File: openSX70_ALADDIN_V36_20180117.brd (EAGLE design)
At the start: 95.9 x 27.9 mm, 42 parts, among them Q1 5.8A/30V/35mΩ, Q2 5.8A/30V/35mΩ, U1 ATMEGA328P_TQFP, U3 BH1750FVI-TR, Y1 CSTCE16M0V53-R0

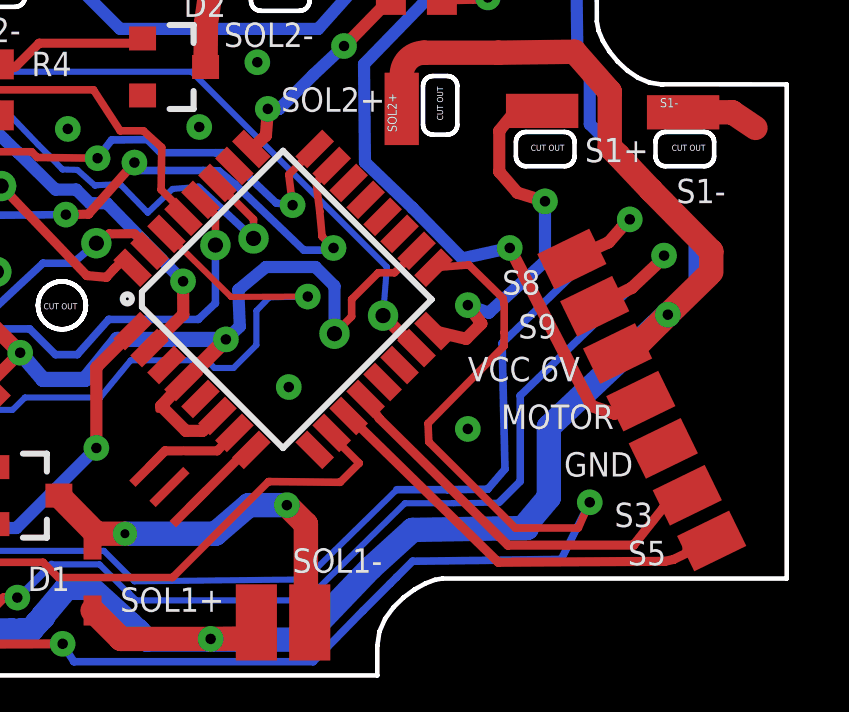
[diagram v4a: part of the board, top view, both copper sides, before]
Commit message: Added TP to pins 15 16 and 17, for bootloader programming (?)
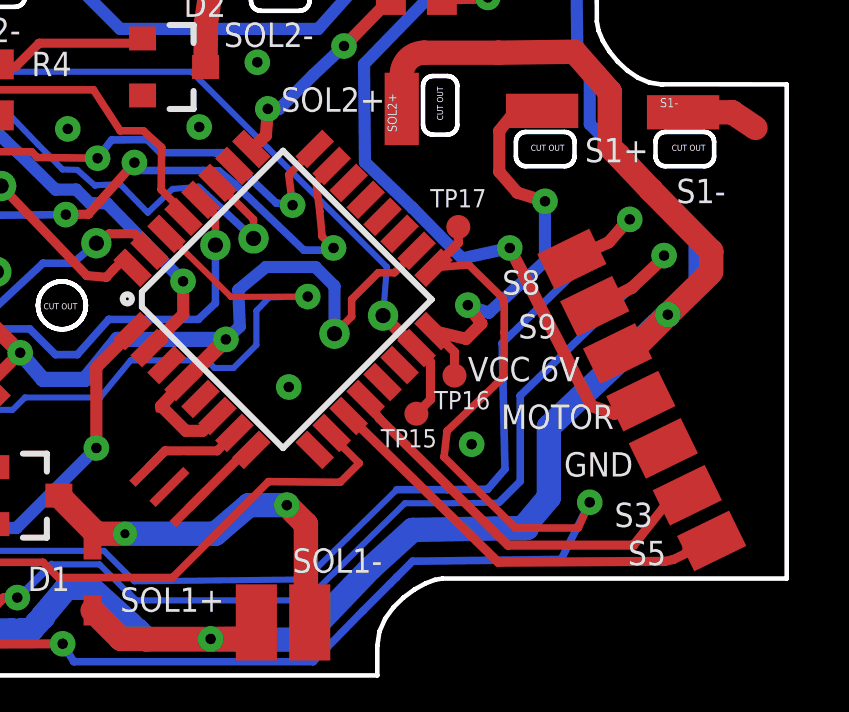
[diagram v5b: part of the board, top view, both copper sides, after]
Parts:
- added TP15, TP16, TP17: PTR1TP08R, testpad:TP08R
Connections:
- net LED: now also TP17.TP
- net S1: now also TP16.TP
- net SOL2: now also TP15.TP
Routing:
- net SOL2: track 26.3 -> 28.9 mm
- net S1: track 12.9 -> 14.7 mm
- net LED: track 92.3 -> 93.6 mm
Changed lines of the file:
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@@
 <element name="TP-3.3V" library="openSX70" package="SX70-S-PAD2" value="SX70-S-PAD-NEW" x="14.351" y="4.064" rot="R90"/>
 <element name="TP-GND" library="openSX70" package="SX70-S-PAD2" value="SX70-S-PAD-NEW" x="12.192" y="4.064" rot="R90"/>
+<element name="TP15" library="testpad" library_urn="urn:adsk.eagle:library:385" package="TP08R" package3d_urn="urn:adsk.eagle:package:27956/1" value="PTR1TP08R" x="85.598" y="11.938" smashed="yes">
+<attribute name="NAME" x="84.409" y="10.8141" size="0.6096" layer="25" font="vector" ratio="12"/>
+<attribute name="TP_SIGNAL_NAME" value="" x="85.598" y="10.033" size="1" layer="37"/>
+<attribute name="VALUE" x="85.217" y="11.557" size="0.0254" layer="27"/>
+</element>
+<element name="TP16" library="testpad" library_urn="urn:adsk.eagle:library:385" package="TP08R" package3d_urn="urn:adsk.eagle:package:27956/1" value="PTR1TP08R" x="86.868" y="13.208" smashed="yes">
+<attribute name="NAME" x="86.187" y="12.0841" size="0.6096" layer="25" font="vector" ratio="12"/>
+<attribute name="TP_SIGNAL_NAME" value="" x="86.868" y="11.303" size="1" layer="37"/>
+<attribute name="VALUE" x="86.487" y="12.827" size="0.0254" layer="27"/>
+</element>
+<element name="TP17" library="testpad" library_urn="urn:adsk.eagle:library:385" package="TP08R" package3d_urn="urn:adsk.eagle:package:27956/1" value="PTR1TP08R" x="86.995" y="18.161" smashed="yes">
+<attribute name="NAME" x="86.06" y="18.8151" size="0.6096" layer="25" font="vector" ratio="12"/>
+<attribute name="TP_SIGNAL_NAME" value="" x="86.995" y="16.256" size="1" layer="37"/>
+<attribute name="VALUE" x="86.614" y="17.78" size="0.0254" layer="27"/>
+</element>
 </elements>
 <signals>
@@
 <wire x1="88.9" y1="22.0345" x2="89.789" y2="22.032" width="0.4064" layer="1"/>
 <wire x1="88.36025" y1="20.0025" x2="88.36025" y2="21.36775" width="0.4064" layer="1"/>
+<contactref element="TP16" pad="TP"/>
+<wire x1="86.168225" y1="14.692571875" x2="86.868" y2="13.992796875" width="0.3048" layer="1"/>
+<wire x1="86.868" y1="13.992796875" x2="86.868" y2="13.208" width="0.3048" layer="1"/>
 </signal>
 <signal name="LED">
@@
 <wire x1="90.9955" y1="8.128" x2="88.9" y2="8.128" width="0.254" layer="1"/>
 <wire x1="90.9955" y1="8.128" x2="91.3765" y2="8.98525" width="0.254" layer="1"/>
-<wire x1="88.52423125" y1="14.64641875" x2="88.519" y2="14.19225" width="0.254" layer="1"/>
-<wire x1="88.519" y1="14.19225" x2="85.98535" y2="11.61415" width="0.254" layer="1"/>
-<wire x1="86.01075" y1="10.99873125" x2="85.98535" y2="11.61415" width="0.254" layer="1"/>
-<wire x1="88.9" y1="8.128" x2="86.01075" y2="10.99873125" width="0.254" layer="1"/>
+<wire x1="88.52423125" y1="14.64641875" x2="88.519" y2="13.17625" width="0.254" layer="1"/>
+<wire x1="88.519" y1="13.17625" x2="86.62035" y2="11.36015" width="0.254" layer="1"/>
+<wire x1="86.51875" y1="10.49073125" x2="86.62035" y2="11.36015" width="0.254" layer="1"/>
+<wire x1="88.9" y1="8.128" x2="86.51875" y2="10.49073125" width="0.254" layer="1"/>
 <wire x1="82.1569" y1="3.6709" x2="83.82" y2="5.3717875" width="0.254" layer="16"/>
 <wire x1="68.1355" y1="1.99225" x2="70.2945" y2="4.2545" width="0.3048" layer="1"/>
+<contactref element="TP17" pad="TP"/>
+<wire x1="86.995" y1="18.161" x2="86.995" y2="17.6302" width="0.3048" layer="1"/>
+<wire x1="86.995" y1="17.6302" x2="86.168225" y2="16.803425" width="0.3048" layer="1"/>
 </signal>
 <signal name="S3">
@@
 <via x="67.31" y="23.8125" extent="1-16" drill="0.508"/>
 <via x="84.48675" y="15.20825" extent="1-16" drill="0.508"/>
+<contactref element="TP15" pad="TP"/>
+<wire x1="85.6025375" y1="14.126884375" x2="86.0679" y2="13.661521875" width="0.3048" layer="1"/>
+<wire x1="86.0679" y1="12.4079" x2="85.598" y2="11.938" width="0.3048" layer="1"/>
+<wire x1="86.0679" y1="13.661521875" x2="86.0679" y2="12.4079" width="0.3048" layer="1"/>
 </signal>
 <signal name="FF">
@@
 <via x="23.495" y="17.78" extent="1-16" drill="0.35"/>
 <via x="22.0345" y="22.0345" extent="1-16" drill="0.35"/>
-<via x="87.3125" y="11.43" extent="1-16" drill="0.35"/>
+<via x="87.4395" y="10.922" extent="1-16" drill="0.35"/>
 <via x="83.08975" y="26.9875" extent="1-16" drill="0.35"/>
 <wire x1="16.41475" y1="9.652" x2="16.5693" y2="9.5279" width="0.2032" layer="16"/>

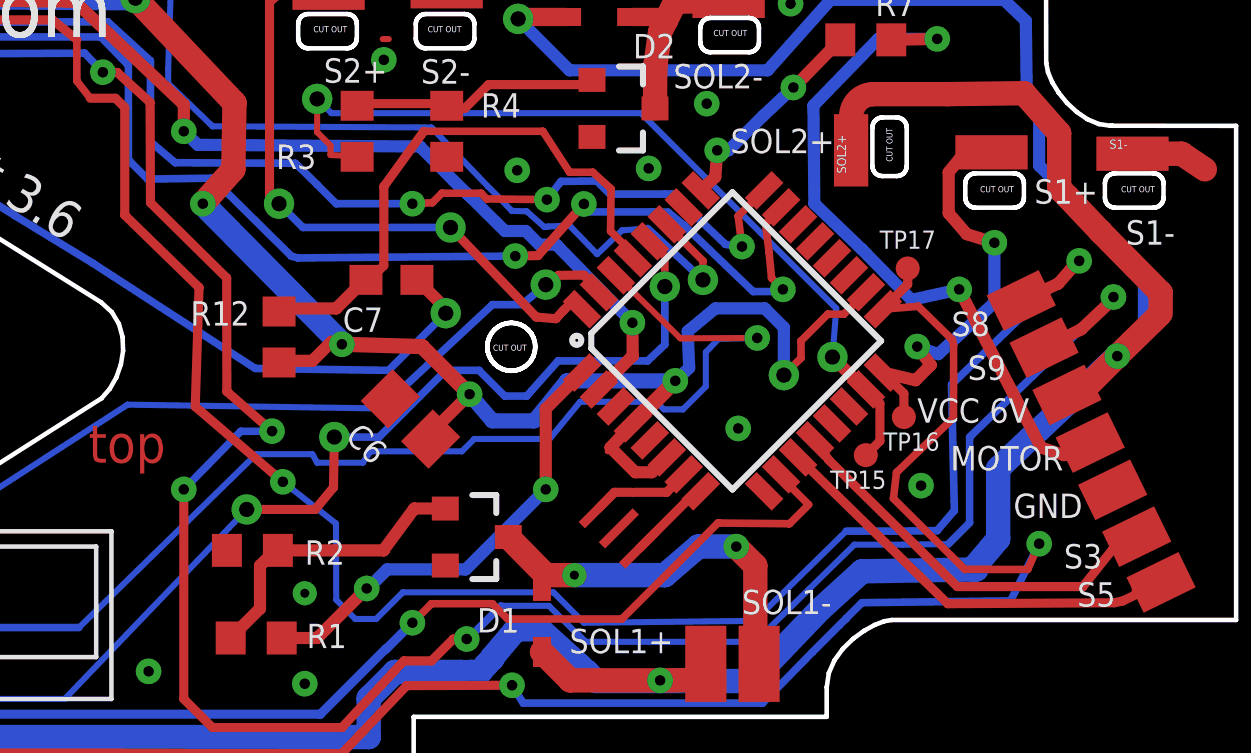
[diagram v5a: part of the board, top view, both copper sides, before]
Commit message: Minor fixes, making the board look nicer.
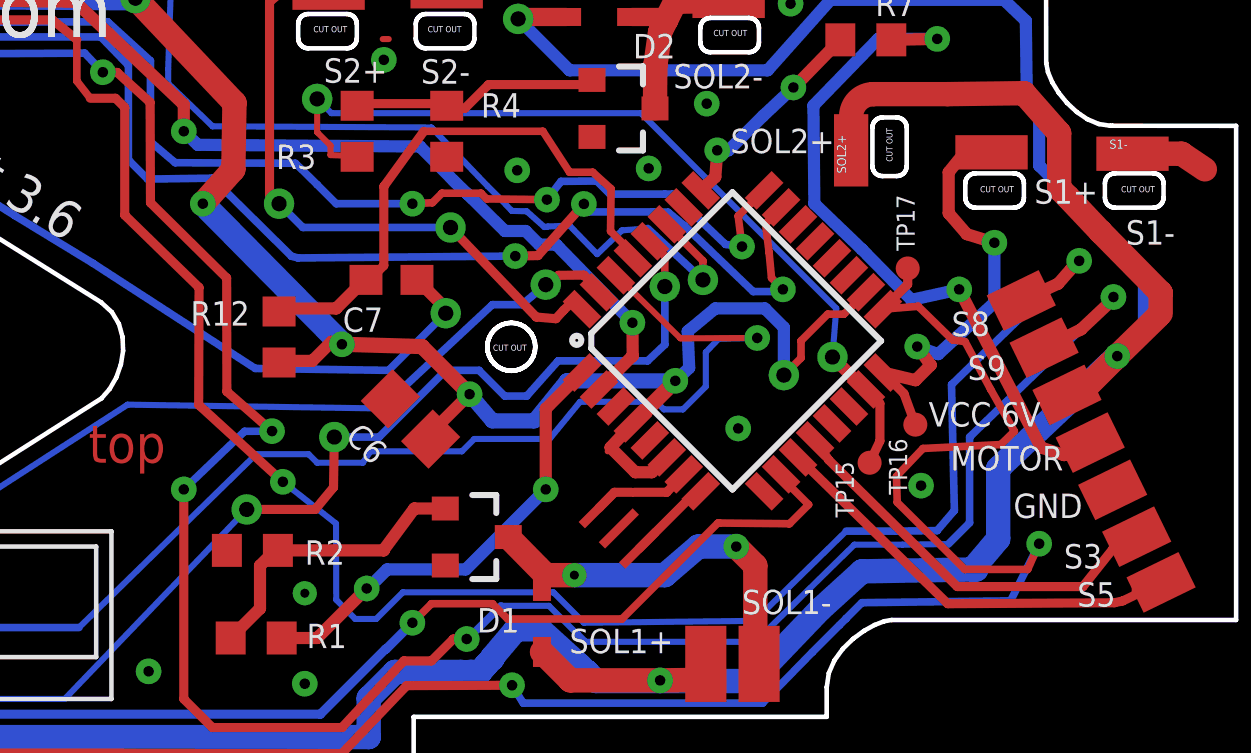
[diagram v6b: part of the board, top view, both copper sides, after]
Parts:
- moved TP16 0.46 mm to (87.2, 13.0)
- moved TP15 0.28 mm to (85.7, 11.7)
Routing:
- net LED: track 93.6 -> 96.5 mm
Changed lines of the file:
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@@
 <text x="90.51925" y="9.8425" size="0.8128" layer="21" font="vector" ratio="20">GND</text>
 <text x="88.42375" y="11.43" size="0.8128" layer="21" font="vector" ratio="20">MOTOR</text>
-<text x="87.3125" y="13.0175" size="0.8128" layer="21" font="vector" ratio="20">VCC 6V</text>
+<text x="87.6935" y="12.8905" size="0.8128" layer="21" font="vector" ratio="20">VCC 6V</text>
 <text x="88.99525" y="14.44625" size="0.8128" layer="21" font="vector" ratio="20">S9</text>
 <text x="88.4555" y="15.90675" size="0.8128" layer="21" font="vector" ratio="20">S8</text>
@@
 <wire x1="59.944" y1="5.207" x2="55.88" y2="5.207" width="0.1524" layer="21"/>
 <wire x1="55.88" y1="5.207" x2="55.88" y2="8.89" width="0.1524" layer="21"/>
+<text x="41.3385" y="24.79675" size="1.27" layer="22" font="vector" ratio="15" rot="R212">"aladdin"</text>
 </plain>
 <attributes>
@@
 <element name="TP-3.3V" library="openSX70" package="SX70-S-PAD2" value="SX70-S-PAD-NEW" x="14.351" y="4.064" rot="R90"/>
 <element name="TP-GND" library="openSX70" package="SX70-S-PAD2" value="SX70-S-PAD-NEW" x="12.192" y="4.064" rot="R90"/>
-<element name="TP15" library="testpad" library_urn="urn:adsk.eagle:library:385" package="TP08R" package3d_urn="urn:adsk.eagle:package:27956/1" value="PTR1TP08R" x="85.598" y="11.938" smashed="yes">
-<attribute name="NAME" x="84.409" y="10.8141" size="0.6096" layer="25" font="vector" ratio="12"/>
-<attribute name="TP_SIGNAL_NAME" value="" x="85.598" y="10.033" size="1" layer="37"/>
-<attribute name="VALUE" x="85.217" y="11.557" size="0.0254" layer="27"/>
-</element>
-<element name="TP16" library="testpad" library_urn="urn:adsk.eagle:library:385" package="TP08R" package3d_urn="urn:adsk.eagle:package:27956/1" value="PTR1TP08R" x="86.868" y="13.208" smashed="yes">
-<attribute name="NAME" x="86.187" y="12.0841" size="0.6096" layer="25" font="vector" ratio="12"/>
-<attribute name="TP_SIGNAL_NAME" value="" x="86.868" y="11.303" size="1" layer="37"/>
-<attribute name="VALUE" x="86.487" y="12.827" size="0.0254" layer="27"/>
+<element name="TP15" library="testpad" library_urn="urn:adsk.eagle:library:385" package="TP08R" package3d_urn="urn:adsk.eagle:package:27956/1" value="PTR1TP08R" x="85.725" y="11.684" smashed="yes">
+<attribute name="NAME" x="85.1979" y="9.86" size="0.6096" layer="25" font="vector" ratio="12" rot="R90"/>
+<attribute name="TP_SIGNAL_NAME" value="" x="85.725" y="9.779" size="1" layer="37"/>
+<attribute name="VALUE" x="85.344" y="11.303" size="0.0254" layer="27"/>
+</element>
+<element name="TP16" library="testpad" library_urn="urn:adsk.eagle:library:385" package="TP08R" package3d_urn="urn:adsk.eagle:package:27956/1" value="PTR1TP08R" x="87.249" y="12.954" smashed="yes">
+<attribute name="NAME" x="86.9759" y="10.622" size="0.6096" layer="25" font="vector" ratio="12" rot="R90"/>
+<attribute name="TP_SIGNAL_NAME" value="" x="87.249" y="11.049" size="1" layer="37"/>
+<attribute name="VALUE" x="86.868" y="12.573" size="0.0254" layer="27"/>
 </element>
 <element name="TP17" library="testpad" library_urn="urn:adsk.eagle:library:385" package="TP08R" package3d_urn="urn:adsk.eagle:package:27956/1" value="PTR1TP08R" x="86.995" y="18.161" smashed="yes">
-<attribute name="NAME" x="86.06" y="18.8151" size="0.6096" layer="25" font="vector" ratio="12"/>
+<attribute name="NAME" x="87.2299" y="18.75" size="0.6096" layer="25" font="vector" ratio="12" rot="R90"/>
 <attribute name="TP_SIGNAL_NAME" value="" x="86.995" y="16.256" size="1" layer="37"/>
 <attribute name="VALUE" x="86.614" y="17.78" size="0.0254" layer="27"/>
@@
 <contactref element="TP16" pad="TP"/>
 <wire x1="86.168225" y1="14.692571875" x2="86.868" y2="13.992796875" width="0.3048" layer="1"/>
-<wire x1="86.868" y1="13.992796875" x2="86.868" y2="13.208" width="0.3048" layer="1"/>
+<wire x1="86.868" y1="13.992796875" x2="87.249" y2="12.954" width="0.3048" layer="1"/>
 </signal>
 <signal name="LED">
@@
 <wire x1="90.424" y1="7.08025" x2="91.3765" y2="8.98525" width="0.254" layer="16"/>
 <wire x1="87.34425" y1="16.898675" x2="88.48725" y2="15.77975" width="0.254" layer="1"/>
-<wire x1="88.48725" y1="15.77975" x2="88.52423125" y2="15.59448125" width="0.254" layer="1"/>
-<wire x1="88.52423125" y1="15.59448125" x2="88.52423125" y2="14.64641875" width="0.254" layer="1"/>
+<wire x1="88.48725" y1="15.77975" x2="88.90523125" y2="15.72148125" width="0.254" layer="1"/>
+<wire x1="88.90523125" y1="15.72148125" x2="89.75725" y2="14.1351" width="0.254" layer="1"/>
+<wire x1="89.75725" y1="14.1351" x2="90.551" y2="12.73395" width="0.254" layer="1"/>
+<wire x1="90.551" y1="12.73395" x2="90.09903125" y2="12.29056875" width="0.254" layer="1"/>
 <wire x1="90.9955" y1="8.128" x2="88.9" y2="8.128" width="0.254" layer="1"/>
 <wire x1="90.9955" y1="8.128" x2="91.3765" y2="8.98525" width="0.254" layer="1"/>
-<wire x1="88.52423125" y1="14.64641875" x2="88.519" y2="13.17625" width="0.254" layer="1"/>
-<wire x1="88.519" y1="13.17625" x2="86.62035" y2="11.36015" width="0.254" layer="1"/>
-<wire x1="86.51875" y1="10.49073125" x2="86.62035" y2="11.36015" width="0.254" layer="1"/>
-<wire x1="88.9" y1="8.128" x2="86.51875" y2="10.49073125" width="0.254" layer="1"/>
+<wire x1="90.09903125" y1="12.29056875" x2="87.503" y2="12.16025" width="0.254" layer="1"/>
+<wire x1="87.503" y1="12.16025" x2="86.62035" y2="11.23315" width="0.254" layer="1"/>
+<wire x1="86.64575" y1="10.36373125" x2="86.62035" y2="11.23315" width="0.254" layer="1"/>
+<wire x1="88.9" y1="8.128" x2="86.64575" y2="10.36373125" width="0.254" layer="1"/>
 <wire x1="82.1569" y1="3.6709" x2="83.82" y2="5.3717875" width="0.254" layer="16"/>
 <wire x1="68.1355" y1="1.99225" x2="70.2945" y2="4.2545" width="0.3048" layer="1"/>
@@
 <contactref element="TP15" pad="TP"/>
 <wire x1="85.6025375" y1="14.126884375" x2="86.0679" y2="13.661521875" width="0.3048" layer="1"/>
-<wire x1="86.0679" y1="12.4079" x2="85.598" y2="11.938" width="0.3048" layer="1"/>
+<wire x1="86.0679" y1="12.4079" x2="85.725" y2="11.684" width="0.3048" layer="1"/>
 <wire x1="86.0679" y1="13.661521875" x2="86.0679" y2="12.4079" width="0.3048" layer="1"/>
 </signal>
@@
 <contactref element="CONN1" pad="3"/>
 <wire x1="79.41945" y1="15.83055" x2="77.37475" y2="17.8435" width="0.2032" layer="1"/>
-<wire x1="65.278" y1="11.96975" x2="67.15125" y2="11.96975" width="0.2032" layer="16"/>
-<wire x1="67.15125" y1="11.96975" x2="67.31" y2="11.684" width="0.2032" layer="16"/>
+<wire x1="65.278" y1="11.96975" x2="67.02425" y2="11.96975" width="0.2032" layer="16"/>
+<wire x1="67.02425" y1="11.96975" x2="67.31" y2="11.684" width="0.2032" layer="16"/>
 <wire x1="67.31" y1="11.684" x2="68.834" y2="11.684" width="0.2032" layer="16"/>
 <wire x1="68.834" y1="11.684" x2="69.088" y2="12.065" width="0.2032" layer="16"/>
@@
 <wire x1="84.9427" y1="9.40435" x2="81.88835" y2="6.4135" width="0.2032" layer="16"/>
 <via x="66.167" y="11.049" extent="1-16" drill="0.35"/>
-<wire x1="63.246" y1="13.55725" x2="66.167" y2="11.049" width="0.3048" layer="1"/>
+<wire x1="63.3603" y1="13.6144" x2="66.167" y2="11.049" width="0.3048" layer="1"/>
 <wire x1="75.184" y1="7.366" x2="70.1675" y2="7.366" width="0.2032" layer="16"/>
 <wire x1="76.2" y1="6.35" x2="75.184" y2="7.366" width="0.2032" layer="16"/>
@@
 <wire x1="60.5889" y1="23.83435" x2="59.74581875" y2="23.83435" width="0.3048" layer="1"/>
 <wire x1="59.2991" y1="24.40806875" x2="59.2991" y2="25.7909" width="0.254" layer="1"/>
-<wire x1="63.373" y1="17.526" x2="63.246" y2="13.55725" width="0.3048" layer="1"/>
+<wire x1="63.373" y1="17.526" x2="63.3603" y2="13.6144" width="0.3048" layer="1"/>
 </signal>
 <signal name="S9@6V">
@@
 <wire x1="62.865" y1="3.81" x2="62.865" y2="10.795" width="0.3048" layer="1"/>
 <via x="62.865" y="10.795" extent="1-16" drill="0.35"/>
-<wire x1="62.865" y1="10.795" x2="64.76365" y2="12.73175" width="0.254" layer="16"/>
-<wire x1="64.76365" y1="12.73175" x2="65.80505" y2="12.7381" width="0.254" layer="16"/>
+<wire x1="62.865" y1="10.795" x2="64.89065" y2="12.73175" width="0.254" layer="16"/>
+<wire x1="64.89065" y1="12.73175" x2="65.80505" y2="12.7381" width="0.254" layer="16"/>
 <via x="65.80505" y="12.7381" extent="1-16" drill="0.35"/>
 <wire x1="65.80505" y1="12.7381" x2="64.3001" y2="14.0589" width="0.3048" layer="1"/>

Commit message: Minor changes, also added TP SCL and SDA. Created gerbers.
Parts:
- added TP-SCL, TP-SDA: PTR1TP08R, testpad:TP08R
- moved TP17 0.92 mm to (87.5, 18.9)
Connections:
- net SCL: now also TP-SCL.TP
- net SDA: now also TP-SDA.TP
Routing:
- net SCL: track 80.3 -> 85.8 mm, vias 3 -> 4
- net SDA: track 102.2 -> 106.3 mm
- net GND: track 8.06 -> 5.49 mm
- net S9@6V: track 111.3 -> 109.5 mm
- net LED: track 96.5 -> 97.3 mm
- net 6V: track 198.8 -> 198.1 mm
